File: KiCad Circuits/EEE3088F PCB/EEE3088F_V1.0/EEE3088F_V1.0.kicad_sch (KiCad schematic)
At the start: 55 parts, among them J1 Conn_01x02_Pin, J2 Conn_02x16_Odd_Even, U1 MT3608, U10 HX SS12D10G6-WJ, U11 HUSB237-AA001-DN06R, U2 INA219AxD, U3 DRV8833PWP, U4 AP2112K-3.3, U5 DRV8833PWP, U6 BQ24074RGT, U7 AP2171W, U8 AP2171W, U9 FSW3157YSOT363G/TR

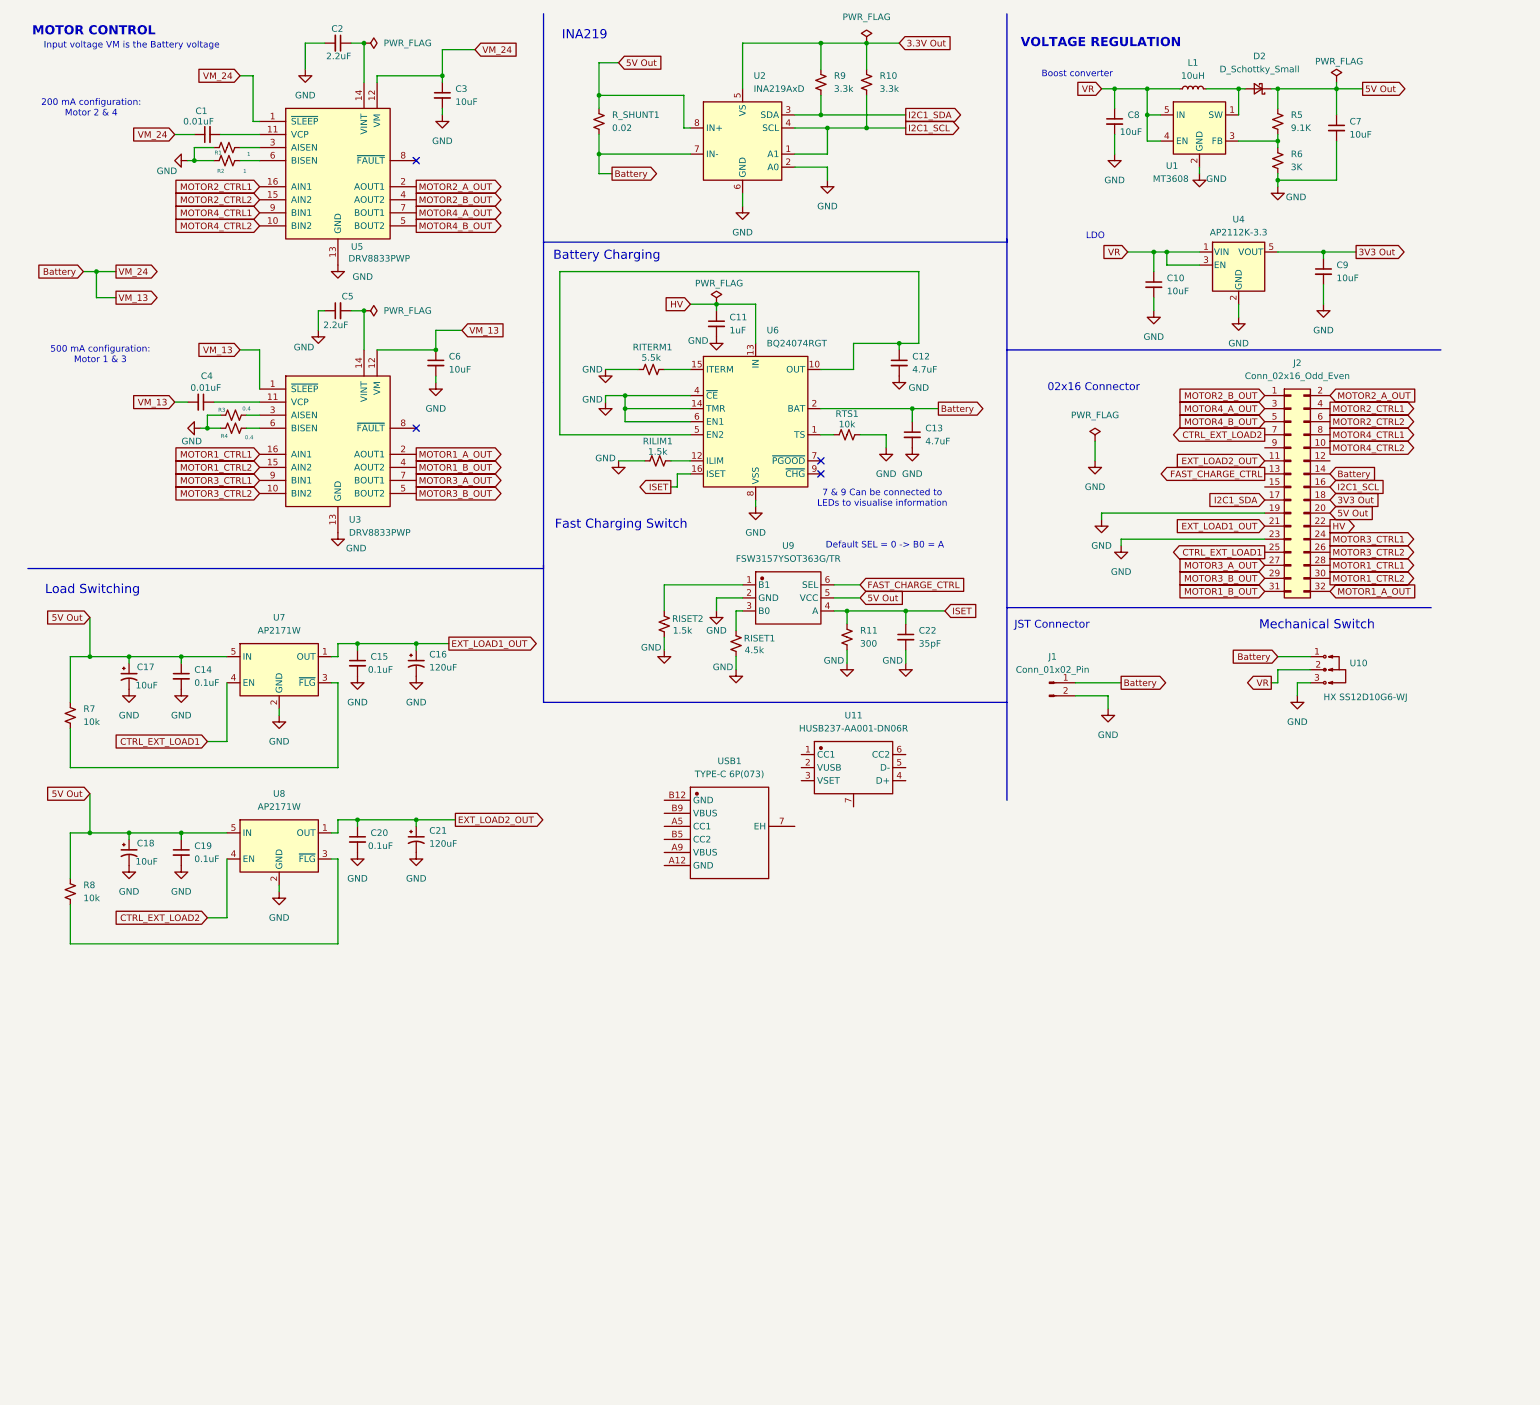
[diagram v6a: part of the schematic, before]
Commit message: bigger page, added USB stuff
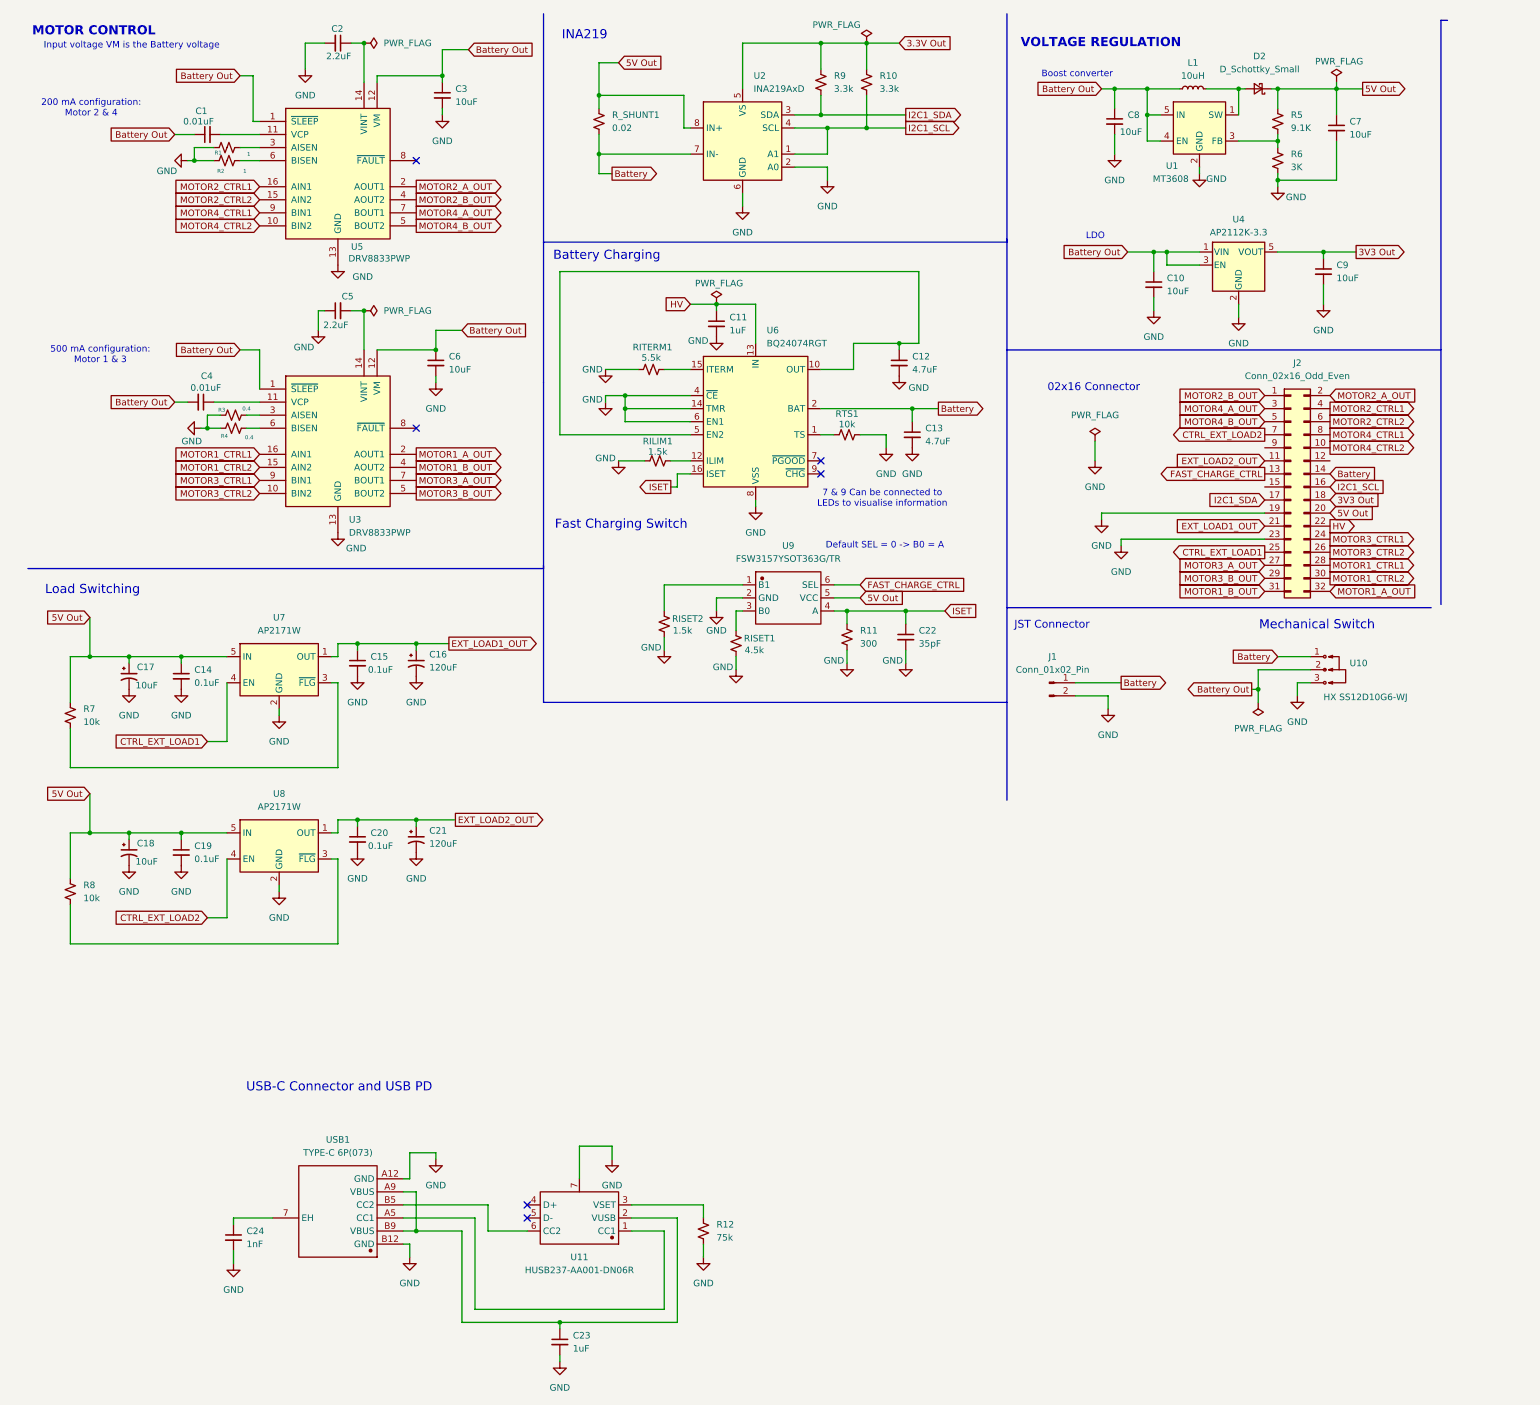
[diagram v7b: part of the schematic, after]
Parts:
- added C23: 1uF, symbol Device:C_Small
- added C24: 1nF, symbol Device:C_Small
- added R12: 75k, symbol Device:R_Small_US
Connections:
- net Battery: no longer C1.1, C3.1, C4.2, C6.1, U3.1 (~{SLEEP}), U3.12 (VM), U5.1 (~{SLEEP}), U5.12 (VM)
- net GND: now also U11.7 (GND), USB1.A12 (GND), USB1.B12 (GND), C23.2, C24.2, R12.2
- net at U11.1 (CC1): now also USB1.A5 (CC1)
- net at U11.2 (VUSB): now also USB1.A9 (VBUS), USB1.B9 (VBUS), C23.1
- net at U11.3 (VSET): now also R12.1
- net at U11.6 (CC2): now also USB1.B5 (CC2)
- net at USB1.7 (EH): now also C24.1
- net VR renamed Battery Out
- net Battery Out: now also C1.1, C3.1, C4.2, C6.1, U3.1 (~{SLEEP}), U3.12 (VM), U5.1 (~{SLEEP}), U5.12 (VM)
- no-connect marks 4 -> 6
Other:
- note added: "USB-C Connector and USB PD"
- moved on the sheet: U11, USB1

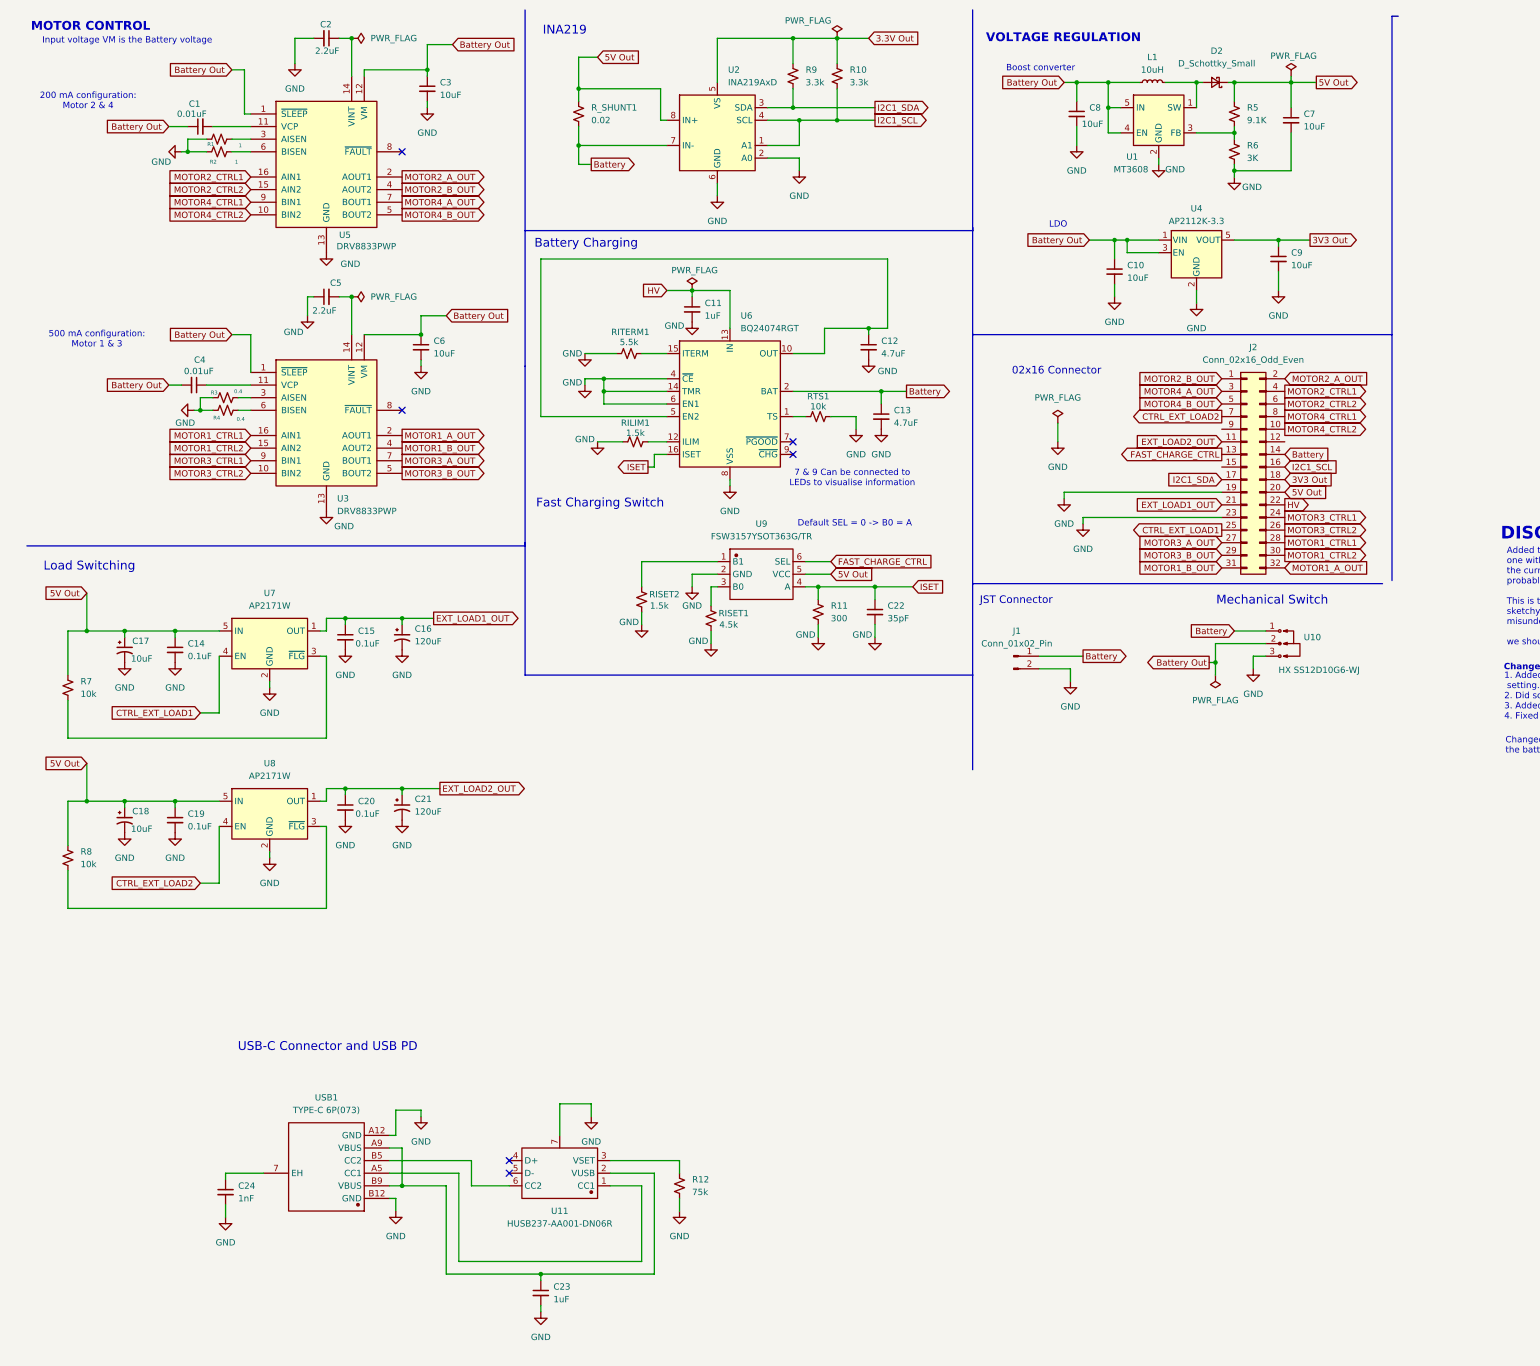
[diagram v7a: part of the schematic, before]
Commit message: Footprints added
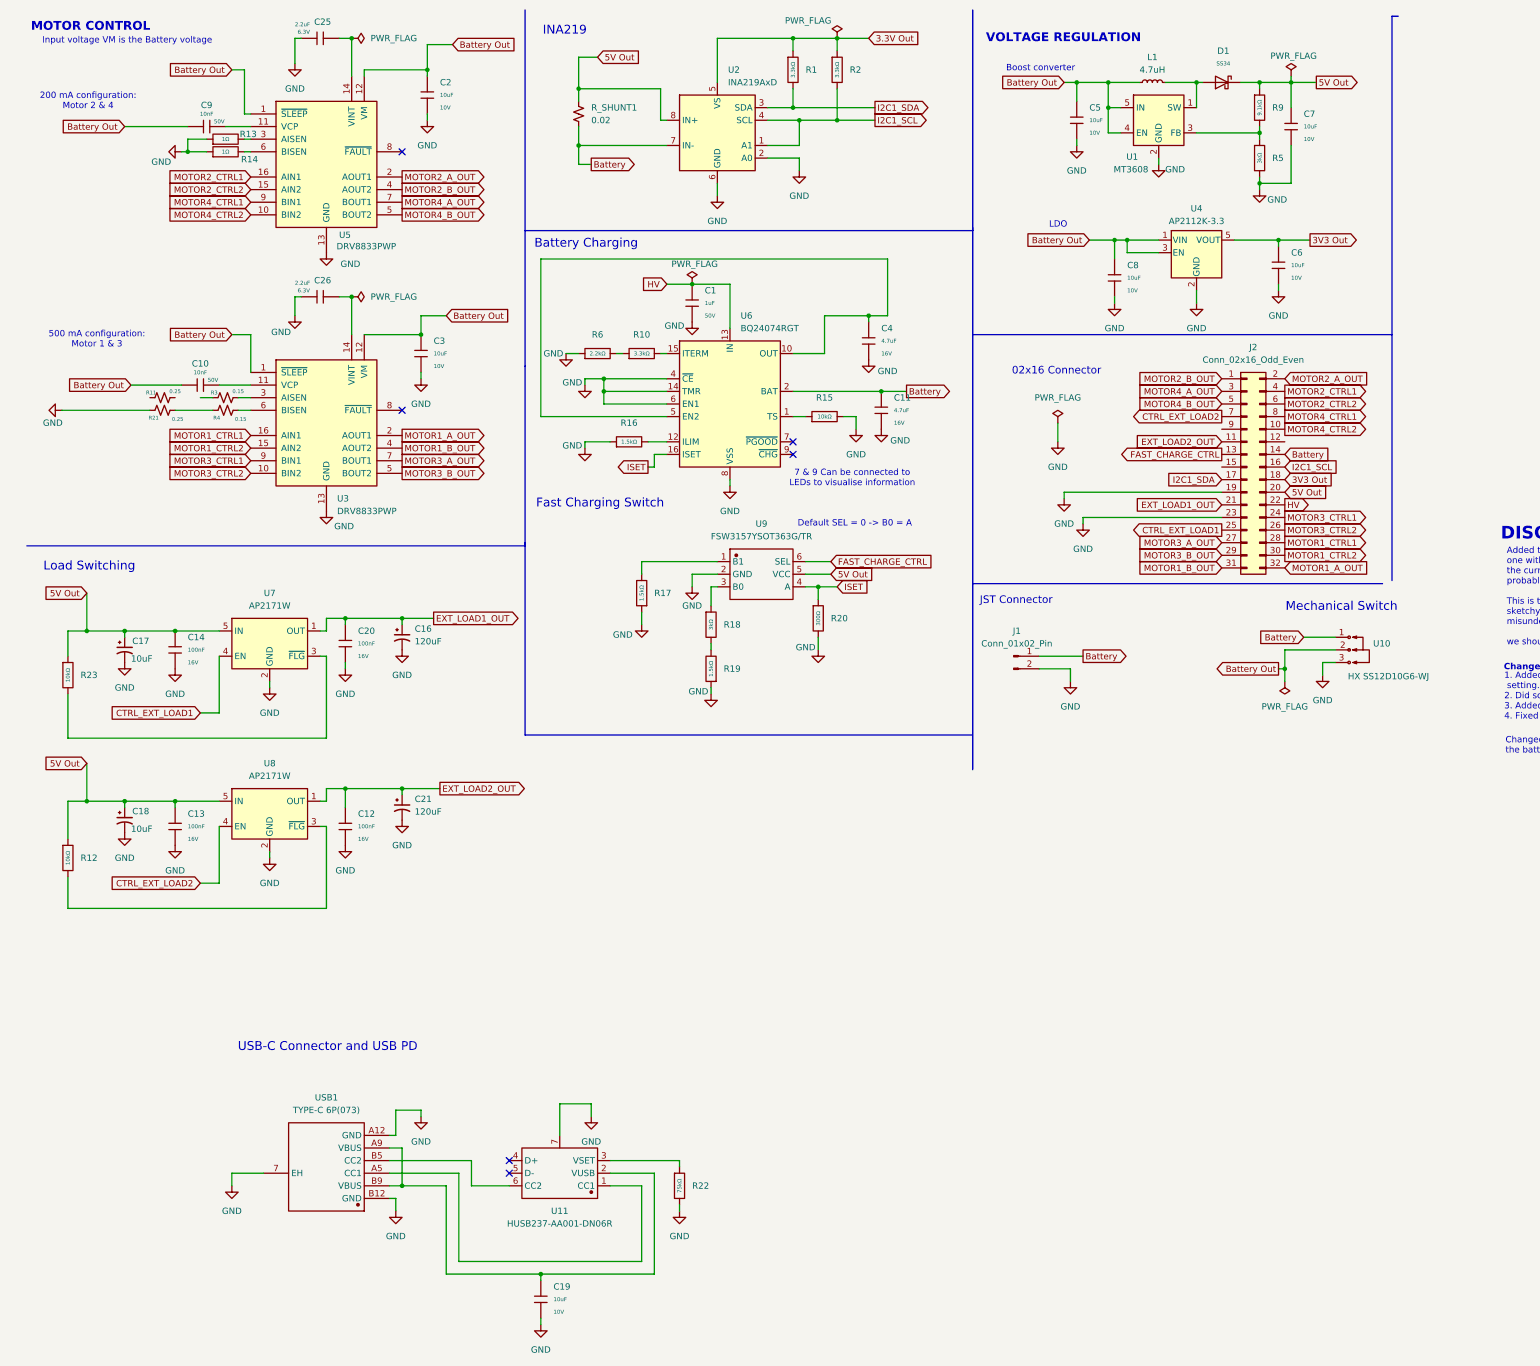
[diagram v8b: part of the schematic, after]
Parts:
- removed C1, C4: 0.01uF, symbol Device:C_Small
- removed C10, C3, C6, C7, C8, C9: 10uF, symbol Device:C_Small
- removed C11, C23: 1uF, symbol Device:C_Small
- removed C12, C13: 4.7uF, symbol Device:C_Small
- removed C14, C15, C19, C20: 0.1uF, symbol Device:C_Small
- removed C2, C5: 2.2uF, symbol Device:C_Small
- removed C22: 35pF, symbol Device:C_Small
- removed C24: 1nF, symbol Device:C_Small
- removed D2: D_Schottky_Small, symbol Device:D_Schottky_Small
- removed R1, R2: 1, symbol Device:R_Small_US
- removed R10, R9: 3.3k, symbol Device:R_Small_US
- removed R12: 75k, symbol Device:R_Small_US
- removed R5: 9.1K, symbol Device:R_Small_US
- removed R6: 3K, symbol Device:R_Small_US
- removed R7, R8, RTS1: 10k, symbol Device:R_Small_US
- removed RILIM1, RISET2: 1.5k, symbol Device:R_Small_US
- removed RISET1: 4.5k, symbol Device:R_Small_US
- removed RITERM1: 5.5k, symbol Device:R_Small_US
- added C1: 1uF, PCM_JLCPCB:C_0603, symbol PCM_JLCPCB-Capacitors:0603,1uF
- added C10, C9: 10nF, PCM_JLCPCB:C_0805, symbol PCM_JLCPCB-Capacitors:0805,10nF
- added C11, C4: 4.7uF, PCM_JLCPCB:C_0603, symbol PCM_JLCPCB-Capacitors:0603,4.7uF
- added C12, C13, C14, C20: 100nF, PCM_JLCPCB:C_0402, symbol PCM_JLCPCB-Capacitors:0402,100nF
- added C19, C2, C3, C5, C6, C7, C8: 10uF, PCM_JLCPCB:C_0603, symbol PCM_JLCPCB-Capacitors:0603,10uF
- added C25, C26: 2.2uF, PCM_JLCPCB:C_0402, symbol PCM_JLCPCB-Capacitors:0402,2.2uF
- added D1: SS34, PCM_JLCPCB:D_SMA, symbol PCM_JLCPCB-Diodes:Schottky,SS34
- added R1, R10, R2: 3.3kΩ, PCM_JLCPCB:R_0603, symbol PCM_JLCPCB-Resistors:0603,3.3kΩ
- added R12, R15, R23: 10kΩ, PCM_JLCPCB:R_0603, symbol PCM_JLCPCB-Resistors:0603,10kΩ
- added R13, R14: 1Ω, PCM_JLCPCB:R_1206, symbol PCM_JLCPCB-Resistors:1206,1Ω
- added R16, R17, R19: 1.5kΩ, PCM_JLCPCB:R_0603, symbol PCM_JLCPCB-Resistors:0603,1.5kΩ
- added R18, R5: 3kΩ, PCM_JLCPCB:R_0603, symbol PCM_JLCPCB-Resistors:0603,3kΩ
- added R20: 300Ω, PCM_JLCPCB:R_0805, symbol PCM_JLCPCB-Resistors:0805,300Ω
- added R21: 0.25, Footprints:R0603, symbol Device:R_Small_US
- added R22: 75kΩ, PCM_JLCPCB:R_0603, symbol PCM_JLCPCB-Resistors:0603,75kΩ
- added R6: 2.2kΩ, PCM_JLCPCB:R_0603, symbol PCM_JLCPCB-Resistors:0603,2.2kΩ
- added R9: 9.1kΩ, PCM_JLCPCB:R_0603, symbol PCM_JLCPCB-Resistors:0603,9.1kΩ
- C16, C21: footprint (none) -> Footprints:CAP-TH_BD8.0-P3.50-D0.6-FD
- C17, C18: footprint (none) -> Footprints:CAP-TH_BD5.0-P2.00-D0.8-FD
- L1: value 10uH -> 4.7uH; footprint (none) -> Footprints:IND-SMD_L2.5-W2.0-VLS252012CX-150M
- R11: value 300 -> 0.25; footprint (none) -> Footprints:R0603
- R3, R4: value 0.4 -> 0.15; footprint (none) -> Footprints:R0603
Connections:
- net 3.3V Out: now also R1.1, R2.1
- net 3V3 Out: now also C6.1
- net 5V Out: now also C13.1, C14.1, C7.1, D1.1, R12.1, R23.1, R9.1
- net Battery: now also C11.1
- net Battery Out: now also C10.1, C2.1, C3.1, C5.1, C8.1, C9.1
- net EXT_LOAD1_OUT: now also C20.1
- net EXT_LOAD2_OUT: now also C12.1
- net GND: now also USB1.7 (EH), C1.2, C11.2, C12.2, C13.2, C14.2, C19.2, C2.2, C20.2, C25.1, C26.1, C3.2, C4.2, C5.2, C6.2, C7.2, C8.2, R13.1, R14.1, R15.2, R16.1, R17.1, R19.1, R20.2, R21.1, R22.2, R5.2, R6.1; no longer R11.2, R3.1, R4.1
- net HV: now also C1.1
- net I2C1_SCL: now also R2.2
- net I2C1_SDA: now also R1.2
- net ISET: now also R20.1; no longer R11.1
- net at U6.15 (ITERM): now also R10.2
- net at U8.3 (~{FLG}): now also R12.2
- net at U6.10 (OUT), U6.11 (OUT), U6.5 (EN2): now also C4.1
- net at U5.14 (VINT): now also C25.2
- net at U9.1 (B1): now also R17.2
- net at U9.3 (B0): now also R18.1
- net at U3.11 (VCP): now also C10.2
- net at U3.14 (VINT): now also C26.2
- net at U5.11 (VCP): now also C9.2
- net at U11.2 (VUSB), USB1.A9 (VBUS), USB1.B9 (VBUS): now also C19.1
- net at U11.3 (VSET): now also R22.1
- net at L1.2, U1.1 (SW): now also D1.2
- net at U7.3 (~{FLG}): now also R23.2
- net at U5.6 (BISEN): now also R14.2
- net at U5.3 (AISEN): now also R13.2
- net at U6.12 (ILIM): now also R16.2
- net at U1.3 (FB): now also R5.1, R9.2
- net at U6.1 (TS): now also R15.1
- new net: R18.2, R19.2
- new net: R10.1, R6.2
- new net: R21.2, R4.1
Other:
- moved on the sheet: U10
